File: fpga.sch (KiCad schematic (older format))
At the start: 69 parts, among them SW1 SW_DIP_x04, SW2 FORCE_VIDEO, U10 74LVC541A, U12 TC7SZ125FU, U5 74LVC14A, U6 74LVC14A, U7 74LVC14A, U9 MAX10-EVAL

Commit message: A lotta fixes
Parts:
- removed R42, R43, R44, R45: R, Resistor_SMD:R_0805_2012Metric_Pad1.20x1.40mm_HandSolder, symbol bkm-68x-simple-rescue:R
- removed SW1: SW_DIP_x04, Button_Switch_SMD:SW_DIP_SPSTx04_Slide_9.78x12.34mm_W8.61mm_P2.54mm, symbol Switch:SW_DIP_x04
- U10: footprint Housings_SSOP:TSSOP-20_4.4x6.5mm_Pitch0.65mm -> Package_SO:TSSOP-20_4.4x6.5mm_P0.65mm
- U12: footprint Package_TO_SOT_SMD:SOT-23-5_HandSoldering -> Package_TO_SOT_SMD:SOT-353_SC-70-5_Handsoldering
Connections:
- net labels removed: FORCE_VIDEO_BIT0, FORCE_VIDEO_BIT1, FORCE_VIDEO_BIT2, FORCE_VIDEO_BIT3
- wire segments 73 -> 66
- no-connect marks 8 -> 15
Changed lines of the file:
@@
 F 0 "U10" H 2600 6325 50  0000 C BNN
 F 1 "74LVC541A" H 2600 5175 50  0000 C TNN
-F 2 "Housings_SSOP:TSSOP-20_4.4x6.5mm_Pitch0.65mm" H 2600 5750 50  0001 C CNN
+F 2 "Package_SO:TSSOP-20_4.4x6.5mm_P0.65mm" H 2600 5750 50  0001 C CNN
 F 3 "" H 2600 5750 50  0001 C CNN
 	1    2600 5750
@@
 F 0 "U12" H 5250 4500 60  0000 C CNN
 F 1 "TC7SZ125FU" H 5250 4100 60  0000 C CNN
-F 2 "Package_TO_SOT_SMD:SOT-23-5_HandSoldering" H 5300 4300 60  0001 C CNN
+F 2 "Package_TO_SOT_SMD:SOT-353_SC-70-5_Handsoldering" H 5300 4300 60  0001 C CNN
 F 3 "" H 5300 4300 60  0001 C CNN
 	1    5250 4300
@@
 RGB_COMP_X
 $Comp
-L Switch:SW_DIP_x04 SW1
-U 1 1 604E9DB2
-P 5350 5800
-F 0 "SW1" H 5350 6267 50  0000 C CNN
-F 1 "SW_DIP_x04" H 5350 6176 50  0000 C CNN
-F 2 "Button_Switch_SMD:SW_DIP_SPSTx04_Slide_9.78x12.34mm_W8.61mm_P2.54mm" H 5350 5800 50  0001 C CNN
-F 3 "~" H 5350 5800 50  0001 C CNN
-	1    5350 5800
-	1    0    0    -1
-$EndComp
-$Comp
 L Switch:SW_SPST SW2
 U 1 1 604F3C48
@@
 	1    0    0    -1
 $EndComp
-Wire Wire Line
-	5050 5600 4950 5600
-Wire Wire Line
-	4950 5600 4950 5700
-Wire Wire Line
-	4950 5700 5050 5700
-Wire Wire Line
-	5050 5800 4950 5800
-Wire Wire Line
-	4950 5800 4950 5700
-Connection ~ 4950 5700
-Wire Wire Line
-	5050 5900 4950 5900
-Wire Wire Line
-	4950 5900 4950 5800
-Connection ~ 4950 5800
-$Comp
-L power:+3.3V #PWR0155
-U 1 1 6051CC90
-P 4800 6400
-F 0 "#PWR0155" H 4800 6250 50  0001 C CNN
-F 1 "+3.3V" V 4815 6528 50  0000 L CNN
-F 2 "" H 4800 6400 50  0001 C CNN
-F 3 "" H 4800 6400 50  0001 C CNN
-	1    4800 6400
-	0    -1   -1   0
-$EndComp
-$Comp
-L power:+3.3V #PWR0156
-U 1 1 6051D571
-P 4950 5600
-F 0 "#PWR0156" H 4950 5450 50  0001 C CNN
-F 1 "+3.3V" V 4965 5728 50  0000 L CNN
-F 2 "" H 4950 5600 50  0001 C CNN
-F 3 "" H 4950 5600 50  0001 C CNN
-	1    4950 5600
-	0    -1   -1   0
-$EndComp
-Connection ~ 4950 5600
 Text GLabel 5800 6400 2    50   Input ~ 0
 FORCE_VIDEO
-Text GLabel 5950 5600 2    50   Input ~ 0
-FORCE_VIDEO_BIT3
-Text GLabel 5950 5700 2    50   Input ~ 0
-FORCE_VIDEO_BIT2
-Text GLabel 5950 5800 2    50   Input ~ 0
-FORCE_VIDEO_BIT1
-Text GLabel 5950 5900 2    50   Input ~ 0
-FORCE_VIDEO_BIT0
-Text GLabel 8500 4500 0    50   Input ~ 0
-FORCE_VIDEO_BIT3
-Text GLabel 8500 4400 0    50   Input ~ 0
-FORCE_VIDEO_BIT2
-Text GLabel 8500 4300 0    50   Input ~ 0
-FORCE_VIDEO_BIT1
-Text GLabel 8500 4200 0    50   Input ~ 0
-FORCE_VIDEO_BIT0
 Text GLabel 8500 4600 0    50   Input ~ 0
 FORCE_VIDEO
-$Comp
-L bkm-68x-simple-rescue:R R42
-U 1 1 6052B756
-P 5800 5600
-F 0 "R42" V 5800 5400 50  0000 C CNN
-F 1 "R" V 5684 5600 50  0000 C CNN
-F 2 "Resistor_SMD:R_0805_2012Metric_Pad1.20x1.40mm_HandSolder" V 5730 5600 50  0001 C CNN
-F 3 "" H 5800 5600 50  0001 C CNN
-	1    5800 5600
-	0    1    1    0
-$EndComp
-$Comp
-L bkm-68x-simple-rescue:R R43
-U 1 1 6052BBDC
-P 5800 5700
-F 0 "R43" V 5800 5500 50  0000 C CNN
-F 1 "R" V 5684 5700 50  0000 C CNN
-F 2 "Resistor_SMD:R_0805_2012Metric_Pad1.20x1.40mm_HandSolder" V 5730 5700 50  0001 C CNN
-F 3 "" H 5800 5700 50  0001 C CNN
-	1    5800 5700
-	0    1    1    0
-$EndComp
-$Comp
-L bkm-68x-simple-rescue:R R44
-U 1 1 6052BF79
-P 5800 5800
-F 0 "R44" V 5800 5600 50  0000 C CNN
-F 1 "R" V 5684 5800 50  0000 C CNN
-F 2 "Resistor_SMD:R_0805_2012Metric_Pad1.20x1.40mm_HandSolder" V 5730 5800 50  0001 C CNN
-F 3 "" H 5800 5800 50  0001 C CNN
-	1    5800 5800
-	0    1    1    0
-$EndComp
-$Comp
-L bkm-68x-simple-rescue:R R45
-U 1 1 6052D097
-P 5800 5900
-F 0 "R45" V 5800 5700 50  0000 C CNN
-F 1 "R" V 5684 5900 50  0000 C CNN
-F 2 "Resistor_SMD:R_0805_2012Metric_Pad1.20x1.40mm_HandSolder" V 5730 5900 50  0001 C CNN
-F 3 "" H 5800 5900 50  0001 C CNN
-	1    5800 5900
-	0    1    1    0
-$EndComp
 $Comp
 L bkm-68x-simple-rescue:R R?
@@
 Text GLabel 9400 4700 2    50   Input ~ 0
 INT_~EXT~_SYNC
+$Comp
+L power:+3.3V #PWR0155
+U 1 1 6051CC90
+P 4800 6400
+F 0 "#PWR0155" H 4800 6250 50  0001 C CNN
+F 1 "+3.3V" V 4815 6528 50  0000 L CNN
+F 2 "" H 4800 6400 50  0001 C CNN
+F 3 "" H 4800 6400 50  0001 C CNN
+	1    4800 6400
+	0    -1   -1   0
+$EndComp
+NoConn ~ 8500 3900
+NoConn ~ 8500 4000
+NoConn ~ 8500 4100
+NoConn ~ 8500 4200
+NoConn ~ 8500 4300
+NoConn ~ 8500 4400
+NoConn ~ 8500 4500
 Wire Bus Line
 	1300 1000 1300 5900

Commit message: Onboard FPGA, passthroughs and a lot of other stuff
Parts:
- removed C27: C, Capacitor_SMD:C_0805_2012Metric_Pad1.18x1.45mm_HandSolder, symbol Device:C
- removed U9: MAX10-EVAL, max10-eval:max-10-eval, symbol max10-eval:MAX10-EVAL
- added C40, C41, C42, C43, C44, C45, C46, C47, C48, C49: 0.1uF, Capacitor_SMD:C_0603_1608Metric_Pad1.08x0.95mm_HandSolder, symbol Device:C
- added C50, C51, C52, C53: 10pF, Capacitor_SMD:C_0603_1608Metric_Pad1.08x0.95mm_HandSolder, symbol bkm-68x-simple-rescue:C_Small
- added D10, D11, D12, D9: D_Schottky, Diode_SMD:D_SOD-123, symbol Device:D_Schottky
- added D13: DEBUG1, LED_SMD:LED_0805_2012Metric_Pad1.15x1.40mm_HandSolder, symbol Device:LED_Small
- added D14: DEBUG2, LED_SMD:LED_0805_2012Metric_Pad1.15x1.40mm_HandSolder, symbol Device:LED_Small
- added J14: JTAG, Connector_PinHeader_2.54mm:PinHeader_2x05_P2.54mm_Vertical, symbol Connector_Generic:Conn_02x05_Odd_Even
- added R44, R45, R73, R74, R75, R77: 10K, Resistor_SMD:R_0805_2012Metric_Pad1.20x1.40mm_HandSolder, symbol bkm-68x-simple-rescue:R
- added R76: 1K, Resistor_SMD:R_0805_2012Metric_Pad1.20x1.40mm_HandSolder, symbol bkm-68x-simple-rescue:R
- added R78, R79: 22R, Resistor_SMD:R_0805_2012Metric_Pad1.20x1.40mm_HandSolder, symbol bkm-68x-simple-rescue:R
- added R82, R83: 470R, Resistor_SMD:R_0805_2012Metric_Pad1.20x1.40mm_HandSolder, symbol bkm-68x-simple-rescue:R
- added SW1: FORCE_VIDEO, PTS645:PTS645, symbol Switch:SW_SPST
- added U15: 10M08SC, Package_QFP:EQFP-144-1EP_20x20mm_P0.5mm_EP8.93x8.7mm_ThermalVias, symbol bkm-68x-simple-rescue:10M08SC-FPGA_Intel
- added U9: KC2520Z50, Oscillator:Oscillator_SMD_Kyocera_KC2520Z-4Pin_2.5x2.0mm, symbol Oscillator:KC2520Z
- R46: value R -> 10K
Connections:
- net labels added: CLK_50MHz, DBG1, DBG2, FORCE_VIDEO2, TCK, TDI, TDO, TMS
- wire segments 66 -> 114
- no-connect marks 15 -> 65
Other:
- moved on the sheet: C12, C20, C21, C22, R15, R16, R17, R18, R19, R20, R21, R22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

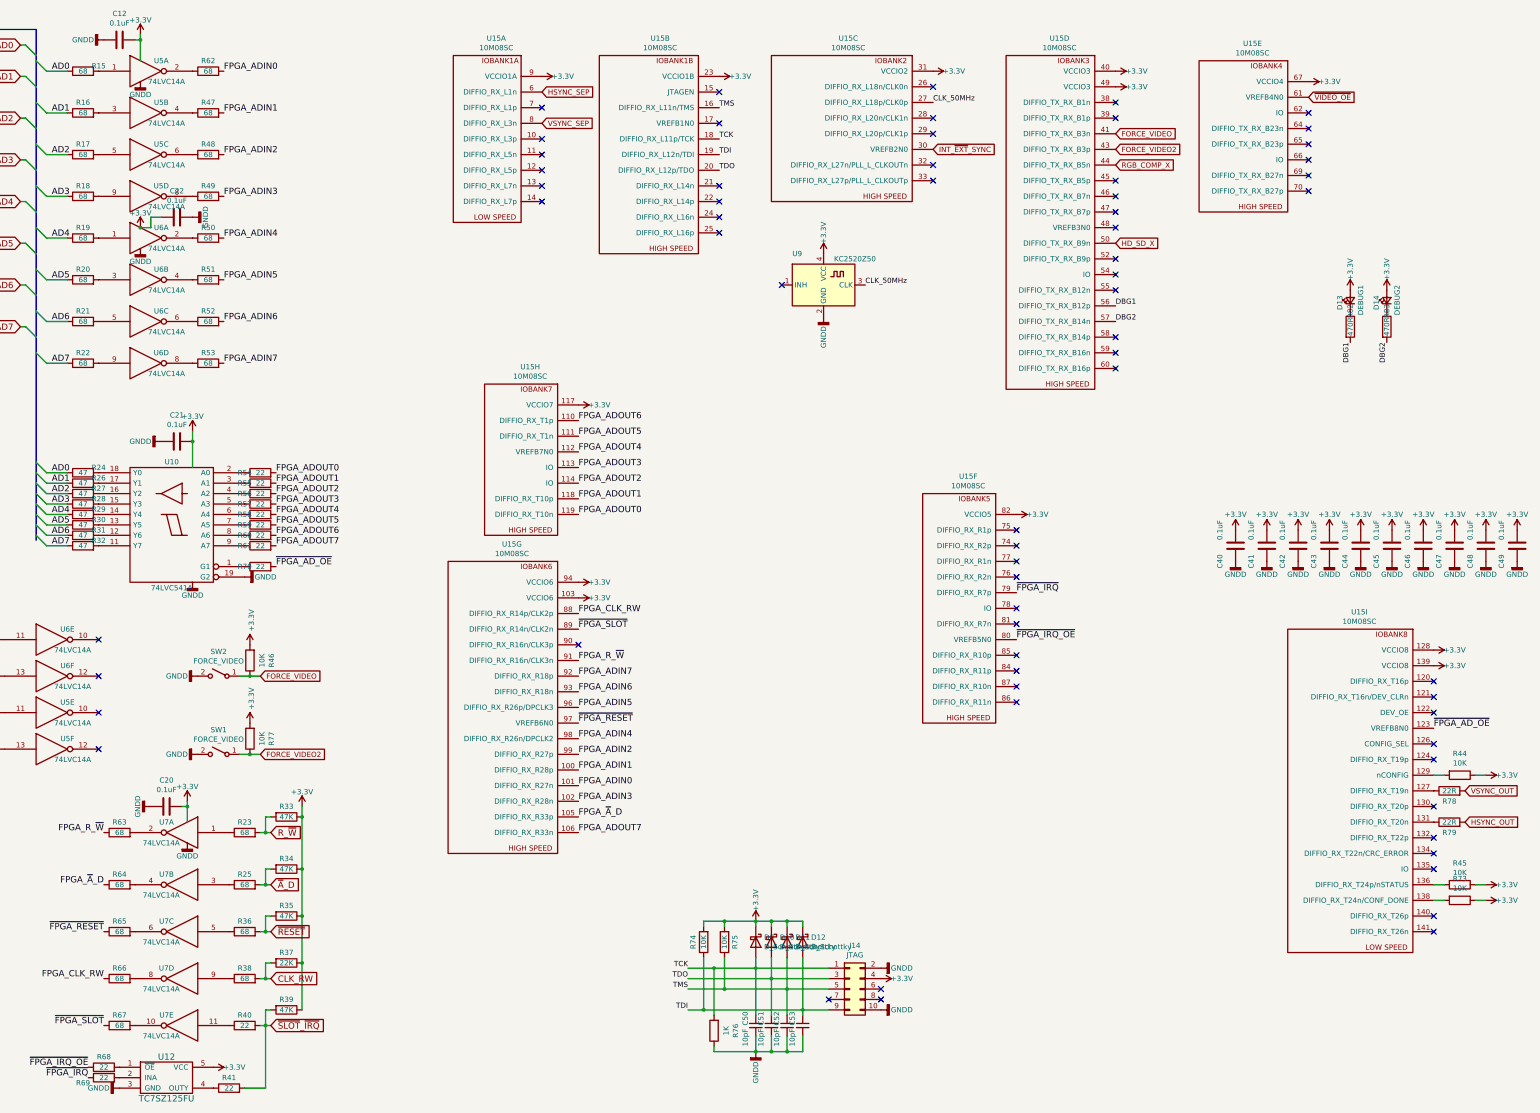
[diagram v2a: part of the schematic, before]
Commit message: Updated some component values
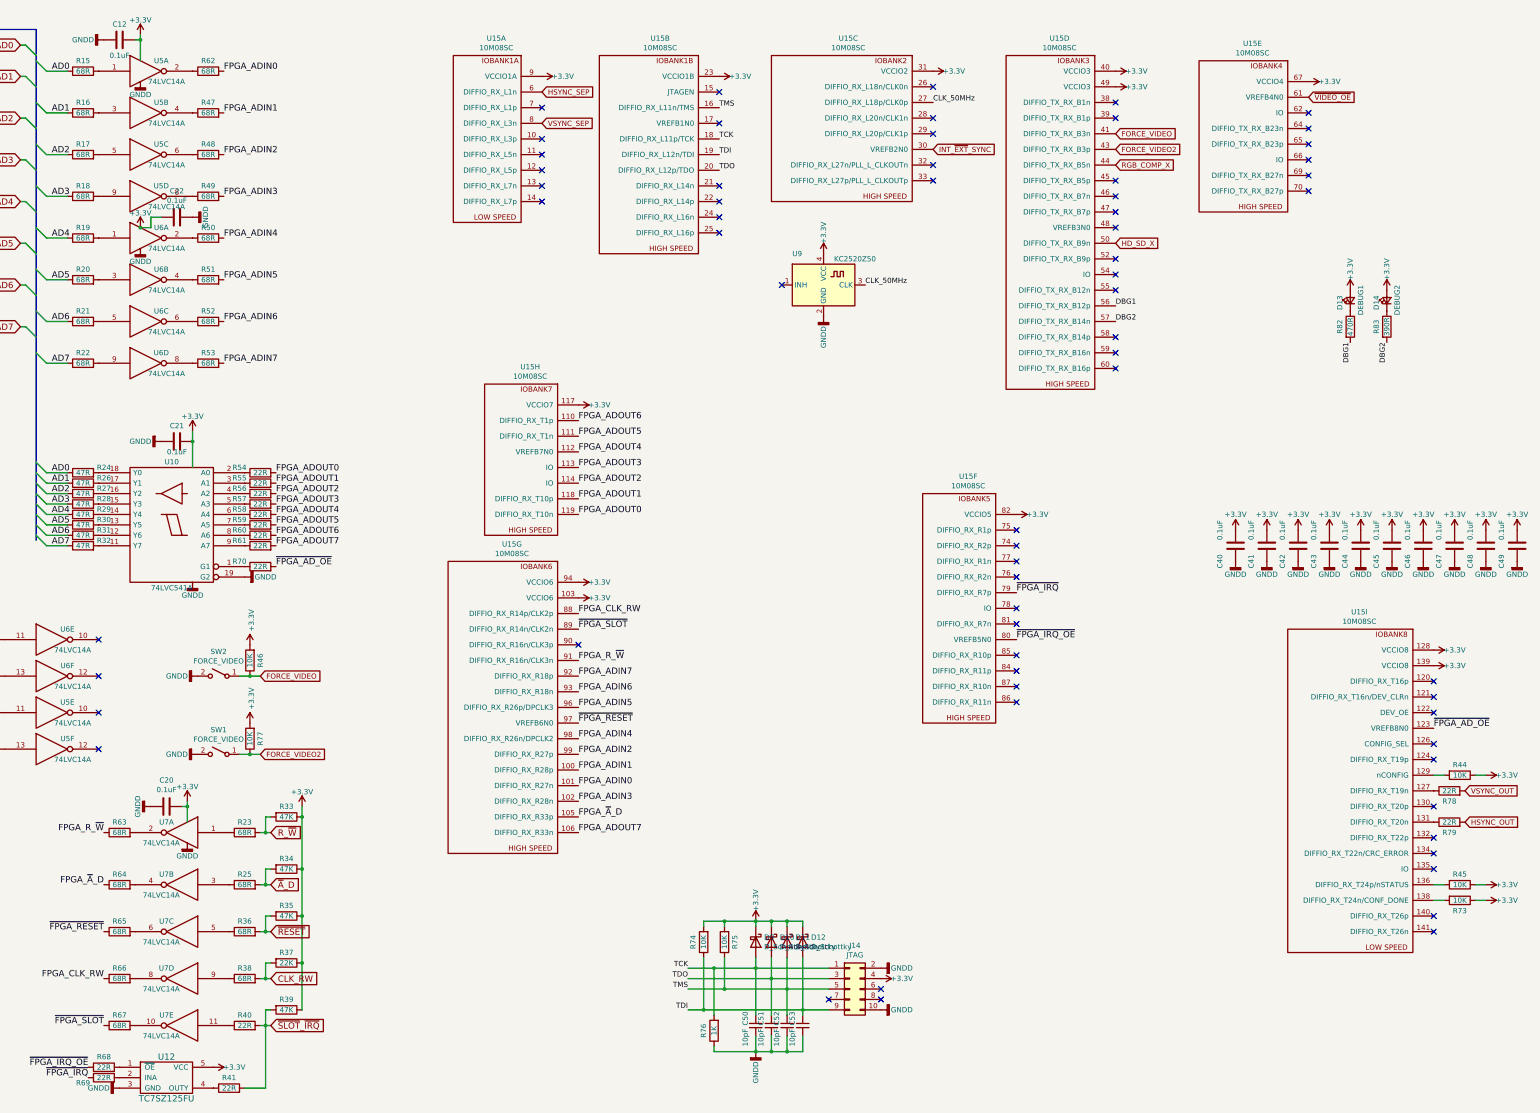
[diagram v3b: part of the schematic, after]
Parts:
- R15, R16, R17, R18, R19, R20, R21, R22, R23, R25, R36, R38, R47, R48, R49, R50, R51, R52, R53, R62, R63, R64, R65, R66, R67: value 68 -> 68R
- R24, R26, R27, R28, R29, R30, R31, R32: value 47 -> 47R
- R40, R41, R54, R55, R56, R57, R58, R59, R60, R61, R68, R69, R70: value 22 -> 22R
- R83: value 470R -> 390R

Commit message: Fixes and additions
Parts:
- added C60: 0.1uF, Capacitor_SMD:C_0603_1608Metric_Pad1.08x0.95mm_HandSolder, symbol Device:C
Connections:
- net +3V3: now also C60.1
- net GND: now also C60.2
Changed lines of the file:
@@
 NoConn ~ 13300 2100
 NoConn ~ 13300 2250
+$Comp
+L Device:C C60
+U 1 1 60A3B6D2
+P 12300 5650
+F 0 "C60" V 12150 5500 50  0000 C CNN
+F 1 "0.1uF" V 12150 5800 50  0000 C CNN
+F 2 "Capacitor_SMD:C_0603_1608Metric_Pad1.08x0.95mm_HandSolder" H 12338 5500 50  0001 C CNN
+F 3 "~" H 12300 5650 50  0001 C CNN
+	1    12300 5650
+	1    0    0    -1
+$EndComp
+$Comp
+L power:+3.3V #PWR0266
+U 1 1 60A3BE26
+P 12300 5500
+F 0 "#PWR0266" H 12300 5350 50  0001 C CNN
+F 1 "+3.3V" H 12300 5650 50  0000 C CNN
+F 2 "" H 12300 5500 50  0001 C CNN
+F 3 "" H 12300 5500 50  0001 C CNN
+	1    12300 5500
+	1    0    0    -1
+$EndComp
+$Comp
+L power:GNDD #PWR0267
+U 1 1 60A3BE30
+P 12300 5800
+F 0 "#PWR0267" H 12300 5550 50  0001 C CNN
+F 1 "GNDD" H 12300 5675 50  0000 C CNN
+F 2 "" H 12300 5800 50  0001 C CNN
+F 3 "" H 12300 5800 50  0001 C CNN
+	1    12300 5800
+	1    0    0    -1
+$EndComp
 Wire Bus Line
 	1100 700  1100 5600

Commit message: Rev. E
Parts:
- added C71: 0.1uF, Capacitor_SMD:C_0805_2012Metric_Pad1.18x1.45mm_HandSolder, symbol Device:C
- added J19: TP_NORM_Y_G, TestPoint:TestPoint_Pad_D2.0mm, symbol bkm-68x-simple-rescue:TEST_1P
- added J20: TP_RGB_COMP_X, TestPoint:TestPoint_Pad_D2.0mm, symbol bkm-68x-simple-rescue:TEST_1P
- added J21: TP_HD_SD_X, TestPoint:TestPoint_Pad_D2.0mm, symbol bkm-68x-simple-rescue:TEST_1P
- added R42, R43: 68R, Resistor_SMD:R_0805_2012Metric_Pad1.20x1.40mm_HandSolder, symbol bkm-68x-simple-rescue:R
- added R87, R88: 22R, Resistor_SMD:R_0805_2012Metric_Pad1.20x1.40mm_HandSolder, symbol bkm-68x-simple-rescue:R
- added U19: 74LVC2G34, Package_TO_SOT_SMD:SOT-23-6_Handsoldering, symbol 74LVCxG34:74LVC2G34
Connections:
- net +3V3: now also C71.2, U19.5 (VCC)
- net GND: now also C71.1, U19.2 (GND)
- net HD_SD_X: now also J21.1
- net HSYNC_SEP: now also U19.1 (1A); no longer U15.6 (DIFFIO_RX_L1n)
- net INT_~EXT~_SYNC: now also R87.2; no longer U15.30 (VREFB2N0)
- net RGB_COMP_X: now also J20.1
- net VSYNC_SEP: now also U19.3 (1A); no longer U15.8 (DIFFIO_RX_L3n)
- net at U15.33 (DIFFIO_RX_L27p/PLL_L_CLKOUTp): now also R88.1
- new net: R87.1, U15.30 (VREFB2N0)
- new net: R42.2, U19.6 (1Y)
- new net: R43.2, U19.4 (1Y)
- new net HSYNC_SEP_BUF: R42.1, U15.6 (DIFFIO_RX_L1n)
- new net NORM_Y_G: J19.1, R88.2
- new net VSYNC_SEP_BUF: R43.1, U15.8 (DIFFIO_RX_L3n)
- no-connect marks 65 -> 64
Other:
- moved on the sheet: U15A, U15B, U15C, U9

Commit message: Rev. E1
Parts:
- D10, D11, D12, D9: value D_Schottky -> NM
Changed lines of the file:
@@
 U 1 1 60BEE0A2
 P 8000 9450
-F 0 "D9" V 7954 9530 50  0000 L CNN
-F 1 "D_Schottky" V 8045 9530 50  0000 L CNN
+F 0 "D9" H 7850 9400 50  0000 L CNN
+F 1 "NM" H 8050 9400 50  0000 L CNN
 F 2 "Diode_SMD:D_SOD-123" H 8000 9450 50  0001 C CNN
 F 3 "~" H 8000 9450 50  0001 C CNN
@@
 U 1 1 60BFCE92
 P 8150 9450
-F 0 "D10" V 8104 9530 50  0000 L CNN
-F 1 "D_Schottky" V 8195 9530 50  0000 L CNN
+F 0 "D10" H 7950 9400 50  0000 L CNN
+F 1 "NM" H 8200 9400 50  0000 L CNN
 F 2 "Diode_SMD:D_SOD-123" H 8150 9450 50  0001 C CNN
 F 3 "~" H 8150 9450 50  0001 C CNN
@@
 U 1 1 60BFDBA6
 P 8300 9450
-F 0 "D11" V 8254 9530 50  0000 L CNN
-F 1 "D_Schottky" V 8345 9530 50  0000 L CNN
+F 0 "D11" H 8100 9400 50  0000 L CNN
+F 1 "NM" H 8350 9400 50  0000 L CNN
 F 2 "Diode_SMD:D_SOD-123" H 8300 9450 50  0001 C CNN
 F 3 "~" H 8300 9450 50  0001 C CNN
@@
 U 1 1 60BFE268
 P 8450 9450
-F 0 "D12" V 8404 9530 50  0000 L CNN
-F 1 "D_Schottky" V 8495 9530 50  0000 L CNN
+F 0 "D12" H 8250 9400 50  0000 L CNN
+F 1 "NM" H 8500 9400 50  0000 L CNN
 F 2 "Diode_SMD:D_SOD-123" H 8450 9450 50  0001 C CNN
 F 3 "~" H 8450 9450 50  0001 C CNN
